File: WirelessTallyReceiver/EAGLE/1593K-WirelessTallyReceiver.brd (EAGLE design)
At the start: 59.4 x 57.8 mm, 9 parts, among them J2 POWER_JACK

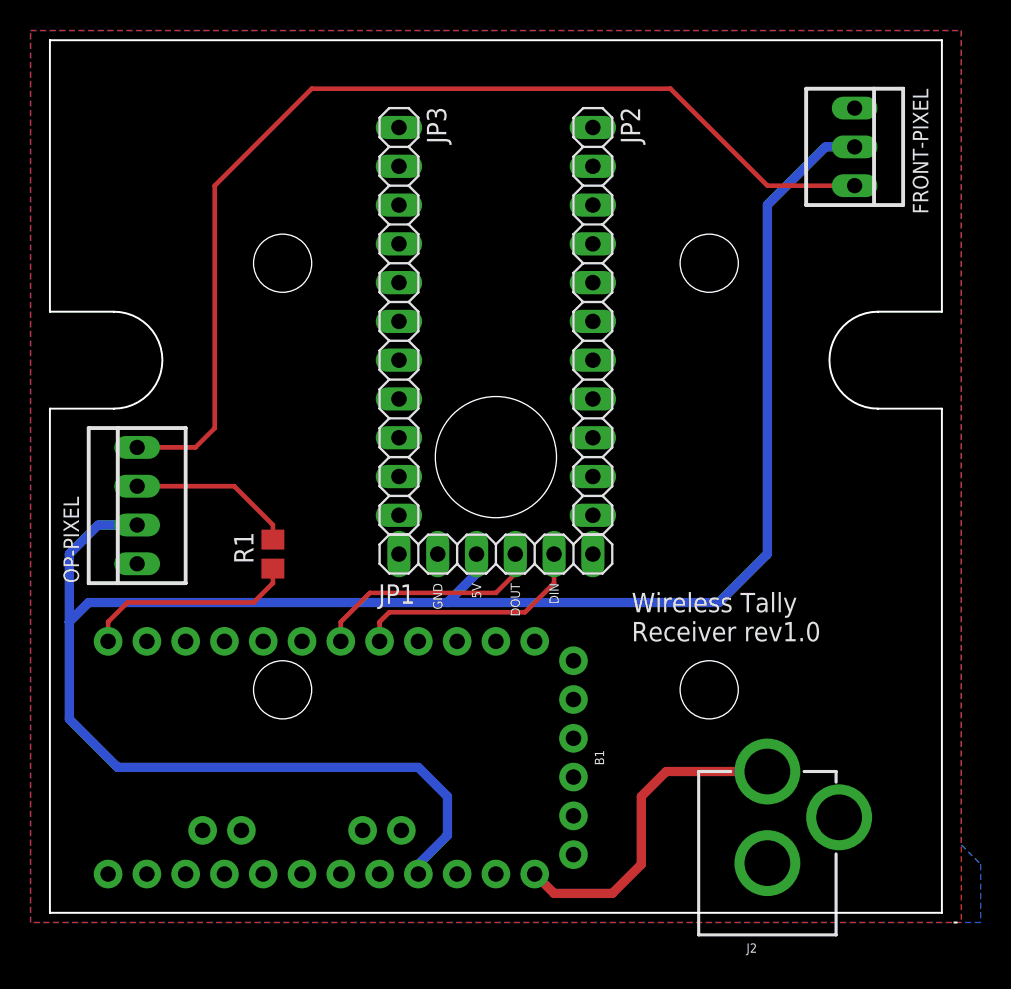
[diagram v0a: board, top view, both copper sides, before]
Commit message: Revisions to boards after working with initial prototypes.
- Update boards to use SMD components to help save on space.
- Redesign wireless receiver to use 3.3v logic to avoid using the Xbee breakout.
- Remove designs that aren't going to be used.
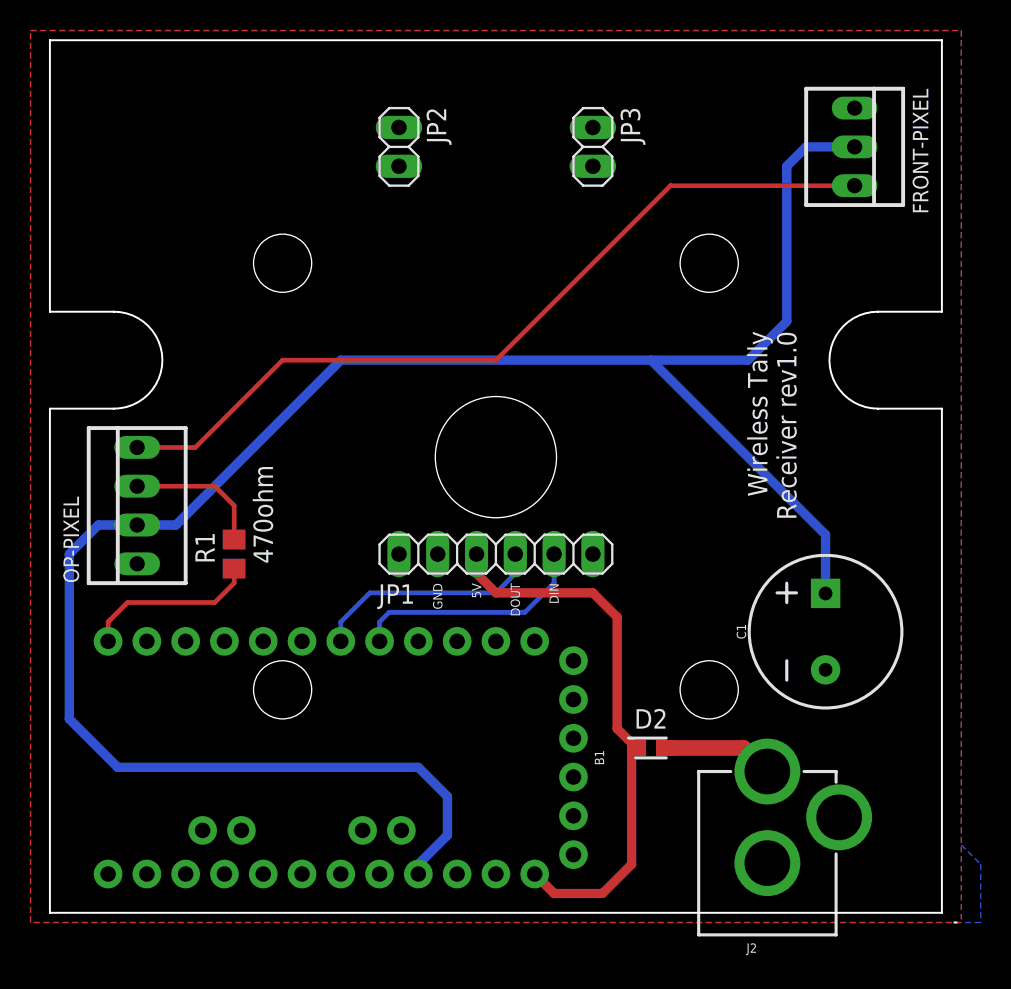
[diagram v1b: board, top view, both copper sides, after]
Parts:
- added C1: 1000uf, SparkFun-Capacitors:CPOL-RADIAL-5MM-10MM
- added D2: ACDBS140-HF, SamacSys_Parts:DIOM2013X100N
- JP2, JP3: device pinhead:1X11 -> pinhead:1X02
- moved JP2 17.1 mm to (24.1, 50.8)
- moved JP3 17.1 mm to (36.8, 50.8)
- moved R1 2.54 mm to (13.3, 24.1)
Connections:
- new net PWR: D2.2, J2.PWR
- net GND: now also C1.-
- net VCC: now also C1.+; no longer JP1.3
- net VIN: now also D2.1, JP1.3; no longer J2.PWR
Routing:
- net NEOCROSS: track 68.7 -> 54.1 mm
- net VIN: track 21.7 -> 36.2 mm
- net PWR: track 0.00 -> 7.31 mm
- net NEOPIXEL: track 14.1 -> 11.5 mm
- net NEOOUT: track 10.9 -> 9.10 mm
- net VCC: track 130.4 -> 132.0 mm
